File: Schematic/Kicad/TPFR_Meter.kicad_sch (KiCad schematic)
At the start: 29 parts, among them J1 PORT, J2 3-pin JST, J3 Conn_01x06_Female, SW1 RST_SW, SW2 MENU, SW3 UP, SW4 DOWN, SW5 ENTER, SW6 SW_SPST, U1 ATmega328-P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

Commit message: updated schematic
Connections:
- net GND: now also DS1.7 (R/~{W})
- no-connect marks 11 -> 10
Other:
- note added: "*Pin 22 is missing on the schematic symbol. It must be connected to ground."
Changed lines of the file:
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@@
   (no_connect (at 147.955 121.285))
   (no_connect (at 195.58 136.525))
-  (no_connect (at 195.58 121.285))
   (no_connect (at 195.58 133.985))
   (no_connect (at 195.58 131.445))
@@
     (stroke (width 0) (type default) (color 0 0 0 0))
   )
+  (wire (pts (xy 195.58 121.285) (xy 192.532 121.285))
+    (stroke (width 0) (type default) (color 0 0 0 0))
+  )
   (wire (pts (xy 167.64 99.06) (xy 163.195 99.06))
     (stroke (width 0) (type default) (color 0 0 0 0))
@@
   )
   (polyline (pts (xy 215.9 97.155) (xy 215.9 99.06))
+    (stroke (width 0) (type default) (color 0 0 0 0))
+  )
+  (wire (pts (xy 192.532 121.285) (xy 192.532 124.46))
     (stroke (width 0) (type default) (color 0 0 0 0))
   )
@@
     (effects (font (size 2 2) (thickness 0.32) bold) (justify left bottom))
   )
+  (text "*Pin 22 is missing on \nthe schematic symbol.\nIt must be connected\nto ground."
+    (at 138.684 161.544 0)
+    (effects (font (size 1.27 1.27)) (justify left bottom))
+  )
   (text "UART " (at 184.15 34.29 0)
     (effects (font (size 2.5 2.5) (thickness 0.5) bold) (justify left bottom))
@@
     )
     (property "Datasheet" "" (id 3) (at 25.4 39.37 0)
+      (effects (font (size 1.27 1.27)) hide)
+    )
+    (pin "1")
+  )
+  (symbol (lib_id "power:GND") (at 192.532 124.46 0) (unit 1)
+    (in_bom yes) (on_board yes)
+    (property "Reference" "#PWR?" (id 0) (at 192.532 130.81 0)
+      (effects (font (size 1.27 1.27)) hide)
+    )
+    (property "Value" "GND" (id 1) (at 192.532 128.27 0))
+    (property "Footprint" "" (id 2) (at 192.532 124.46 0)
+      (effects (font (size 1.27 1.27)) hide)
+    )
+    (property "Datasheet" "" (id 3) (at 192.532 124.46 0)
       (effects (font (size 1.27 1.27)) hide)
     )
@@
       (reference "#PWR0111") (unit 1) (value "VCC") (footprint "")
     )
+    (path "/058baea9-ab80-4250-a7d6-f8cd4151b9a2"
+      (reference "#PWR?") (unit 1) (value "GND") (footprint "")
+    )
     (path "/7a7cc428-1fbd-458c-8b5e-2aa6f0fe19e3"

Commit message: updated schematic
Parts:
- added R2: 680, symbol Device:R
- added R5: 150K, symbol Device:R
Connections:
- net DB5: now also U1.18 (PB4); no longer U1.11 (PD5)
- net GND: now also R5.1
- net at J1.1 (Pin_1), R4.2: now also R2.2, R5.2
- new net T1: R2.1, U1.11 (PD5)
- no-connect marks 10 -> 9
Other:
- moved on the sheet: R4

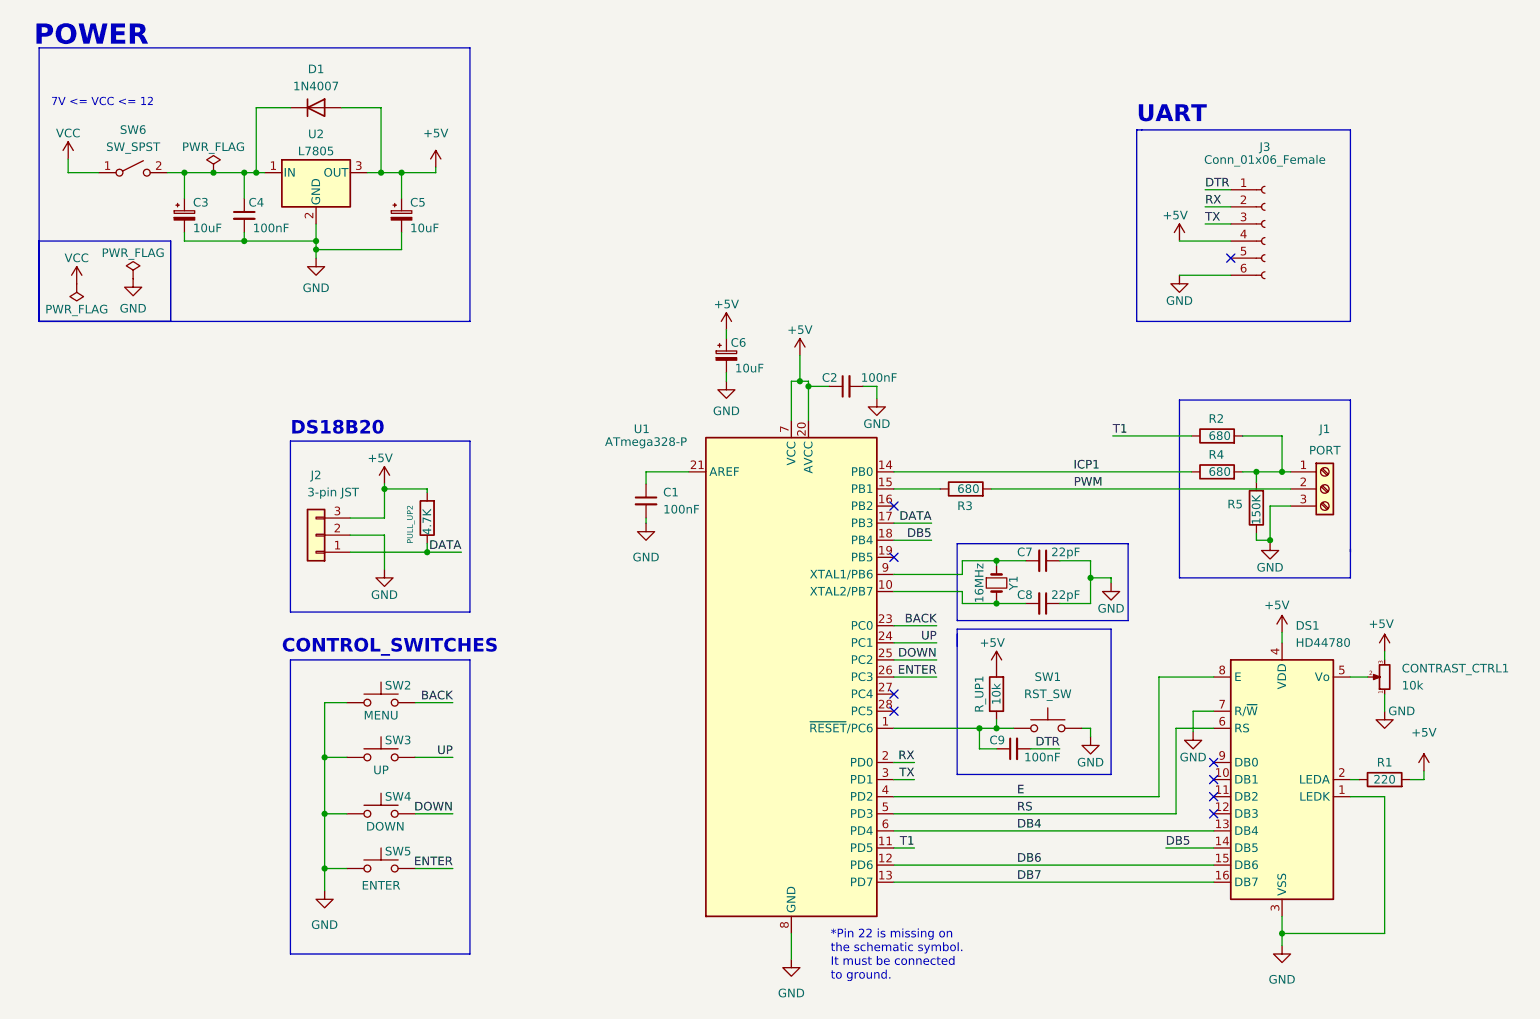
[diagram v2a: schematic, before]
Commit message: updated schematic & footprint
added a barrel jack for power input, updated footprints of the symbol and changed the input switch
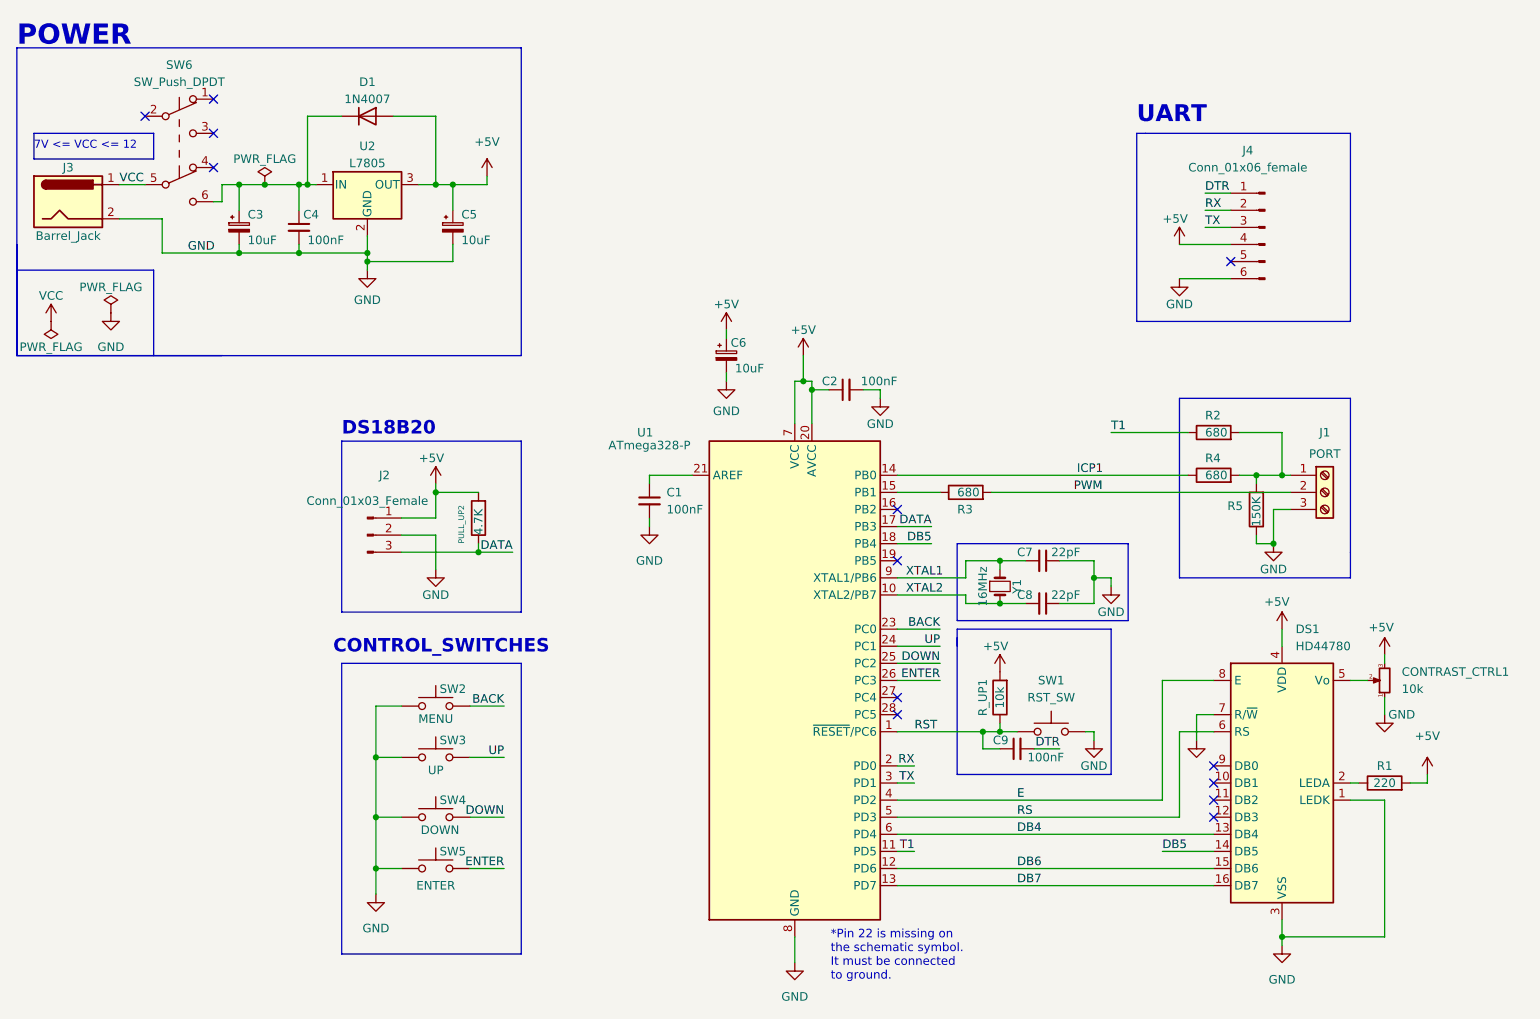
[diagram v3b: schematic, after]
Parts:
- removed J2: 3-pin JST, symbol Connector_Generic:Conn_01x03
- removed J3: Conn_01x06_Female, symbol Connector:Conn_01x06_Female
- removed SW6: SW_SPST, symbol Switch:SW_SPST
- added J2: Conn_01x03_Female, Connector_PinHeader_2.54mm:PinHeader_1x03_P2.54mm_Vertical, symbol Connector:Conn_01x03_Pin
- added J3: Barrel_Jack, Connector_BarrelJack:BarrelJack_Horizontal, symbol Connector:Barrel_Jack
- added J4: Conn_01x06_female, Connector_PinHeader_2.54mm:PinHeader_1x06_P2.54mm_Vertical, symbol Connector:Conn_01x06_Pin
- added SW6: SW_Push_DPDT, Button_Switch_THT:SW_Push_2P2T_Toggle_CK_PVA2xxH1xxxxxxV2, symbol Switch:SW_Push_DPDT
- C1, C2, C4, C7, C8, C9: footprint (none) -> Capacitor_THT:C_Disc_D5.0mm_W2.5mm_P2.50mm
- C3, C5, C6: footprint (none) -> Capacitor_THT:CP_Radial_D5.0mm_P2.50mm
- CONTRAST_CTRL1: footprint (none) -> Potentiometer_THT:Potentiometer_Runtron_RM-065_Vertical
- J1: footprint (none) -> TerminalBlock:TerminalBlock_Altech_AK300-3_P5.00mm
- PULL_UP2, R1, R2, R3, R4, R5, R_UP1: footprint (none) -> Resistor_THT:R_Axial_DIN0207_L6.3mm_D2.5mm_P7.62mm_Horizontal
- SW1, SW2, SW3, SW4, SW5: footprint (none) -> Button_Switch_THT:SW_PUSH_6mm_H4.3mm
- Y1: footprint (none) -> Crystal:Crystal_HC49-4H_Vertical
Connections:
- net +5V: now also J2.1 (Pin_1), J4.4 (Pin_4)
- net DATA: now also J2.3 (Pin_3)
- net DTR: now also J4.1 (Pin_1)
- net GND: now also J2.2 (Pin_2), J3.2, J4.6 (Pin_6)
- net RX: now also J4.2 (Pin_2)
- net TX: now also J4.3 (Pin_3)
- net VCC: now also J3.1, SW6.5 (B)
- net XTAL1: now reaches C7.2, U1.9 (XTAL1/PB6), Y1.1
- net XTAL2: now reaches C8.2, U1.10 (XTAL2/PB7), Y1.2
- net at C3.1, C4.1, D1.1 (K)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: now also SW6.6 (C)
- net RST: now reaches C9.1, R_UP1.1, SW1.1, U1.1 (~{RESET}/PC6)
- no-connect marks 9 -> 13
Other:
- moved on the sheet: C1, C2, C3, C4, C5, C9, CONTRAST_CTRL1, DS1, J1, PULL_UP2, R1, R2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

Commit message: symbols & footprint
updated LCD symbol and footprint, changed UART & dsb18b20 connectors to female sockets
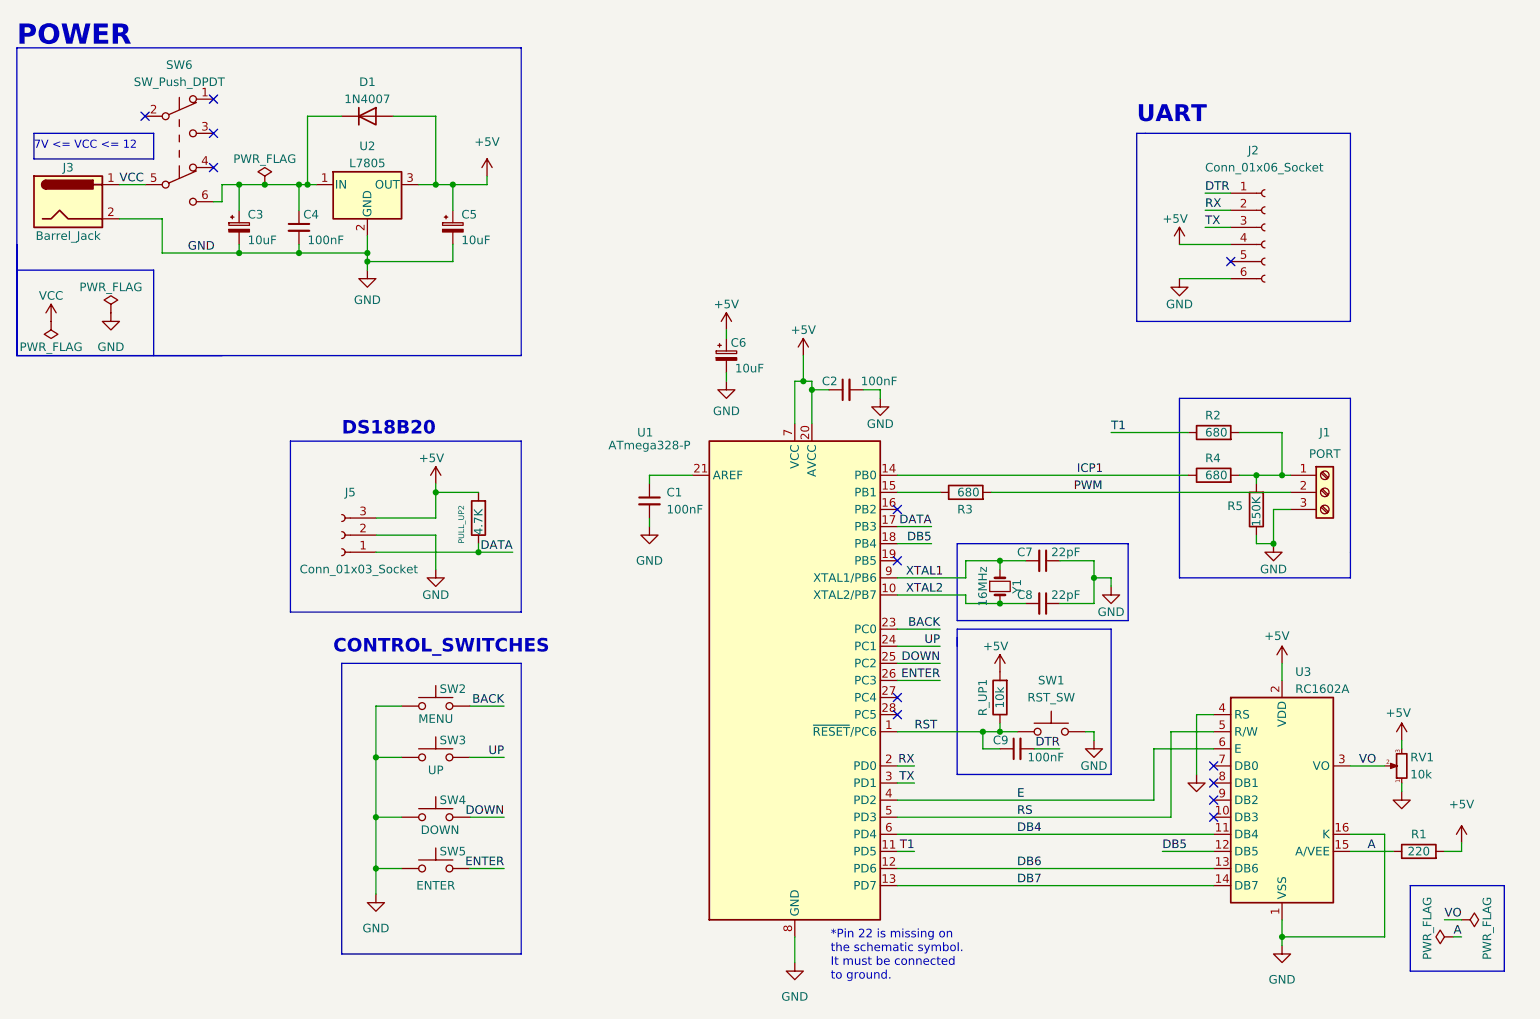
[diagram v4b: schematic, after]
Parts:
- removed DS1: HD44780, Display:HY1602E, symbol Display_Character:HY1602E
- removed J2: Conn_01x03_Female, Connector_PinHeader_2.54mm:PinHeader_1x03_P2.54mm_Vertical, symbol Connector:Conn_01x03_Pin
- removed J4: Conn_01x06_female, Connector_PinHeader_2.54mm:PinHeader_1x06_P2.54mm_Vertical, symbol Connector:Conn_01x06_Pin
- added J2: Conn_01x06_Socket, Connector_PinSocket_2.54mm:PinSocket_1x06_P2.54mm_Horizontal, symbol Connector:Conn_01x06_Socket
- added J5: Conn_01x03_Socket, Connector_PinSocket_2.54mm:PinSocket_1x03_P2.54mm_Vertical, symbol Connector:Conn_01x03_Socket
- added U3: RC1602A, 16x02A_LCD_lib:LCD-1602A, symbol Display_Character:RC1602A
- renumbered CONTRAST_CTRL1 to RV1
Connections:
- net +5V: now also J2.4 (Pin_4), J5.3 (Pin_3), U3.2 (VDD)
- net DATA: now also J5.1 (Pin_1)
- net DB4: now also U3.11 (DB4)
- net DB5: now also U3.12 (DB5)
- net DB6: now also U3.13 (DB6)
- net DB7: now also U3.14 (DB7)
- net DTR: now also J2.1 (Pin_1)
- net E: now also U3.6 (E)
- net GND: now also J2.6 (Pin_6), J5.2 (Pin_2), U3.1 (VSS), U3.16 (K), U3.4 (RS)
- net RS: now also U3.5 (R/W)
- net RX: now also J2.2 (Pin_2)
- net TX: now also J2.3 (Pin_3)
- net A: now reaches R1.1
- net A: now also U3.15 (A/VEE)
- net VO: now reaches RV1.2
- net VO: now also U3.3 (VO)
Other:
- moved on the sheet: R1, RV1
